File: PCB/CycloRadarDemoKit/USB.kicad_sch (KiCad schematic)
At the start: 9 parts, among them J301 USB_C_Receptacle_USB2.0, U301 CP2102N-Axx-xQFN28

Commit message: USB designed with TODOs, ESP part changed
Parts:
- added D302: TX_LED, symbol Device:LED
- added D303: RX_LED, symbol Device:LED
- added Q301, Q302: L8050QLT1G, Package_TO_SOT_SMD:SOT-23, symbol Transistor_BJT:BC817
- added R302: 22.1K(1%), symbol Device:R
- added R303: 47.5K(1%), symbol Device:R
- added R304, R305: ???, symbol Device:R
- added R306, R307: 100K(1%), symbol Device:R
- R301: value 4.7K(1%) -> 1K(1%)
- U301: footprint Package_DFN_QFN:QFN-28-1EP_5x5mm_P0.5mm_EP3.35x3.35mm -> Package_DFN_QFN:QFN-24-1EP_4x4mm_P0.5mm_EP2.6x2.6mm; symbol Interface_USB:CP2102N-Axx-xQFN28 -> Interface_USB:CP2102N-Axx-xQFN24
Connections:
- net +3V3_USB: now also U301.5 (VIO), D302.2 (A), D303.2 (A)
- net EN_AUTO: now also Q301.3 (C)
- net GND: now also U301.2 (GND), U301.25 (GND), R303.2; no longer U301.29 (GND), U301.3 (GND)
- net IO0_AUTO: now also Q302.3 (C)
- net RXD: now also U301.20 (RXD); no longer U301.25 (RXD)
- net TXD: now also U301.21 (TXD); no longer U301.26 (TXD)
- net VBUS: now also R302.1; no longer U301.8 (VBUS)
- net at U301.13 (~{RXT}/GPIO.1): now also R305.1
- net at U301.14 (~{TXT}/GPIO.0): now also R304.1
- net RTS: now reaches U301.19 (~{RTS})
- net RTS: now also Q301.2 (E), R307.1
- net DTR: now reaches U301.23 (~{DTR})
- net DTR: now also Q302.2 (E), R306.1
- net at D301.4 (K), J301.A6 (D+), J301.B6 (D+): now also U301.3 (D+); no longer U301.4 (D+)
- net at D301.3 (K), J301.A7 (D-), J301.B7 (D-): now also U301.4 (D-); no longer U301.5 (D-)
- new net: D303.1 (K), R305.2
- new net: R302.2, R303.1, U301.8 (VBUS)
- new net: Q302.1 (B), R307.2
- new net: Q301.1 (B), R306.2
- new net: D302.1 (K), R304.2
- no-connect marks 5 -> 13
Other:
- note added: "TODO: Choose LEDs and their resistors"
- note removed: "TODO: AUTO BOOT"
- note removed: "TODO: Compare the circuity with the ESP32 module schematics"
- moved on the sheet: C301, C302, C303, C304, D301, FB301, J301, R301

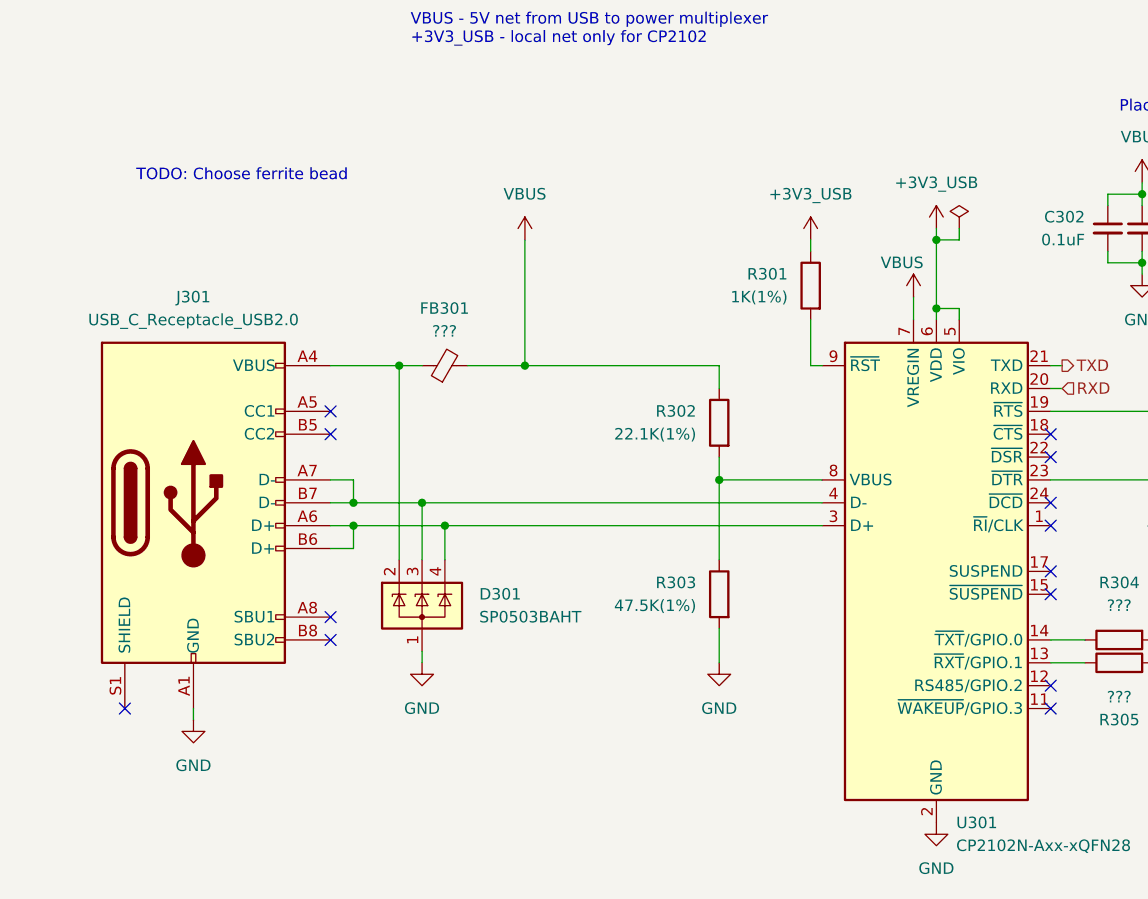
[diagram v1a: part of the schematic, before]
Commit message: Readme, PCB new symbol routed
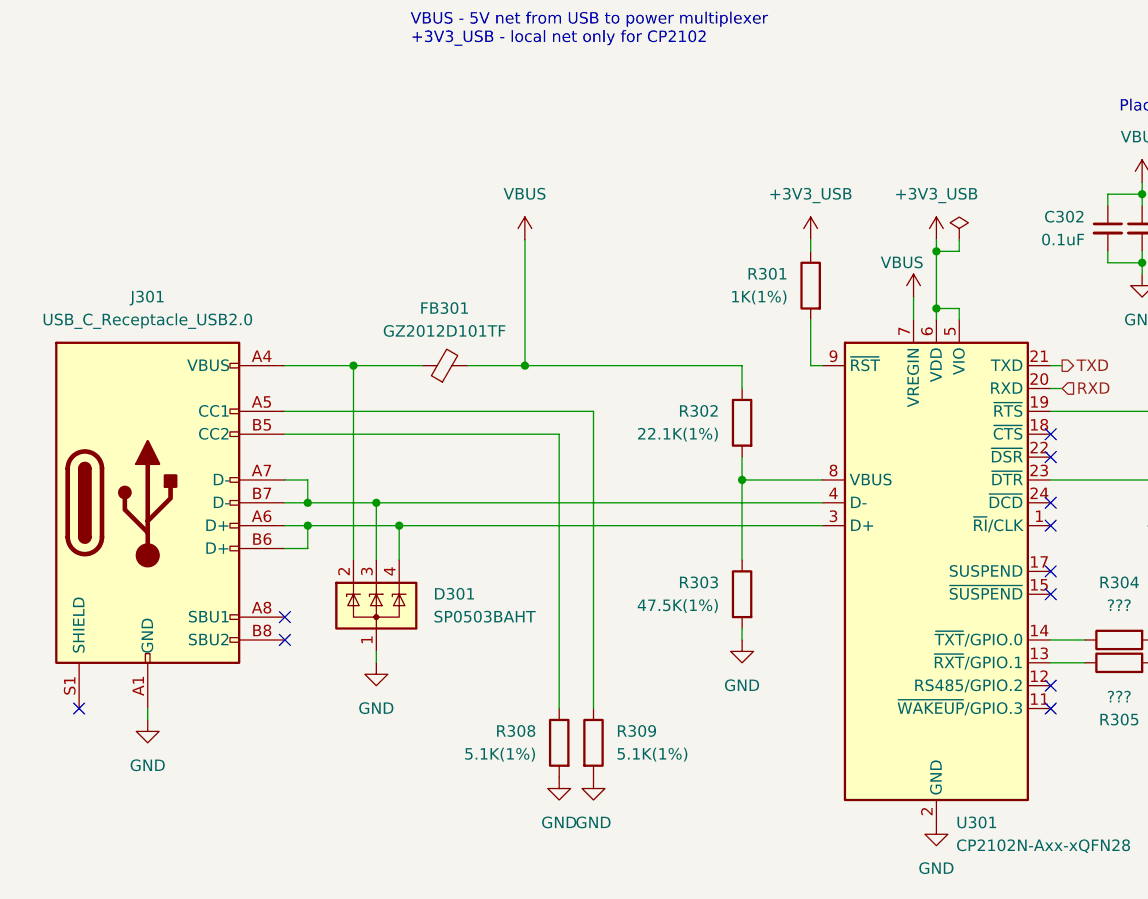
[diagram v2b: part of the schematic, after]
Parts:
- added R308, R309: 5.1K(1%), symbol Device:R
- FB301: value ??? -> GZ2012D101TF
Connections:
- net GND: now also R308.2, R309.2
- net at J301.A5 (CC1): now also R309.1
- net at J301.B5 (CC2): now also R308.1
- no-connect marks 13 -> 11
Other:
- note removed: "TODO: Choose ferrite bead"
- moved on the sheet: D301, J301, R302, R303

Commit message: PCB power manag. WIP
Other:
- note added: "Notes: +3V3_USB - local net only for CP2102 VBUS - 5V net from USB to power multiplexer"
- note removed: "Notes: Max current through VDD: 500mA VBUS - 5V net from USB to power multiplexer +3V3_USB - local net only for CP2102"
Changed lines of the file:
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@@
     (stroke (width 0) (type default))
   )
-  (text "Notes:\nMax current through VDD: 500mA\n\nVBUS - 5V net from USB to power multiplexer\n+3V3_USB - local net only for CP2102"
-    (at 88.9 33.02 0)
+  (text "Notes:\n+3V3_USB - local net only for CP2102\nVBUS - 5V net from USB to power multiplexer"
+    (at 105.41 38.1 0)
     (effects (font (size 1.27 1.27)) (justify left bottom))
   )

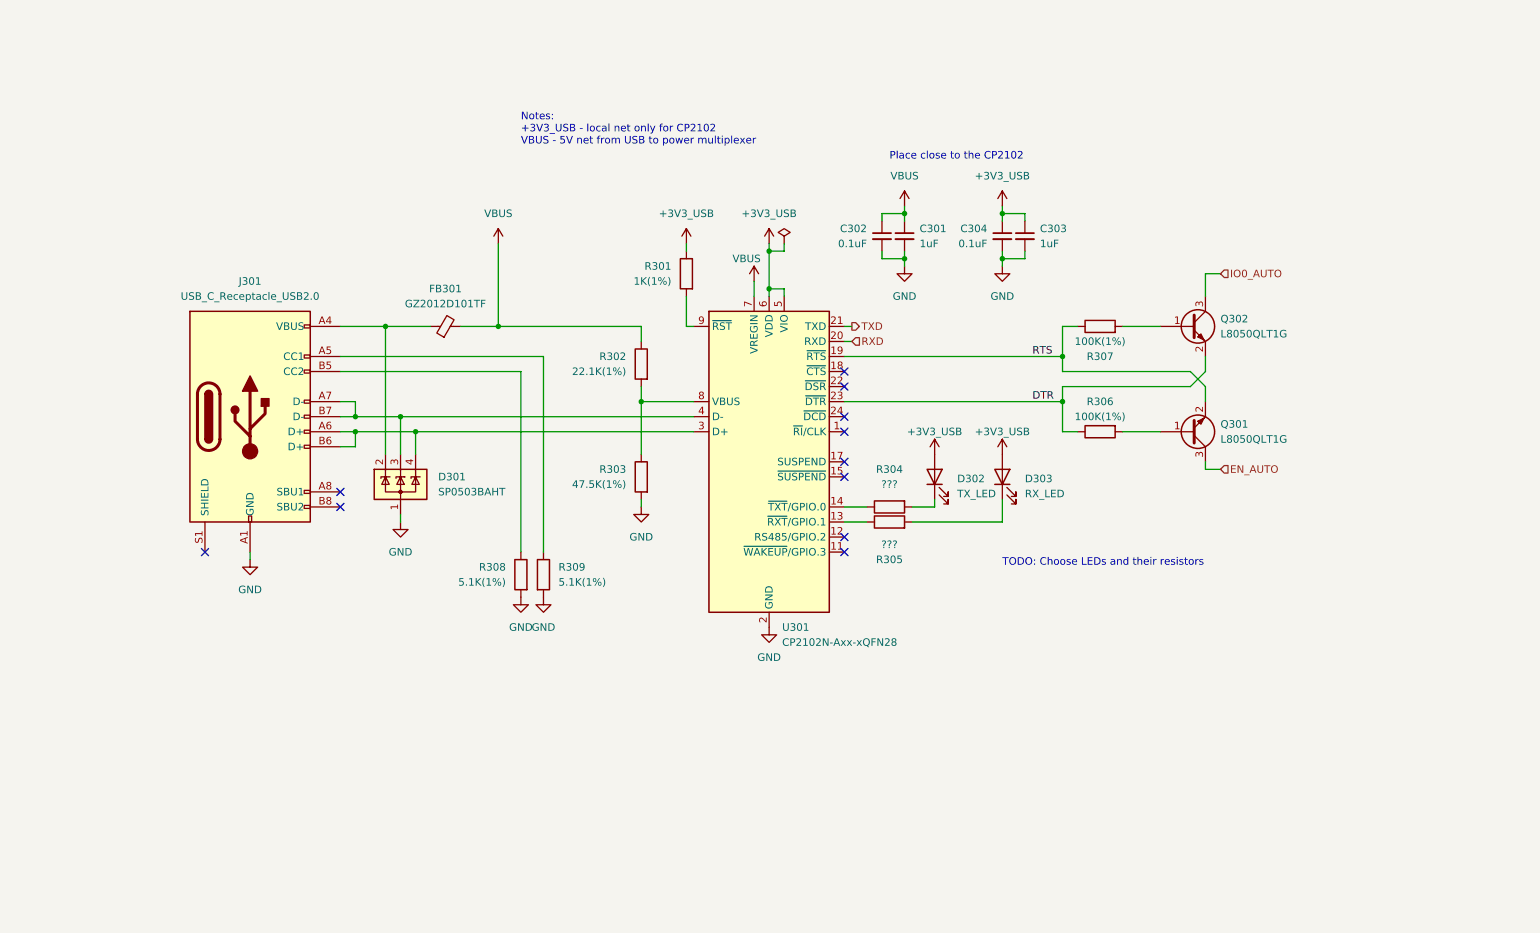
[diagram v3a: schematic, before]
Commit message: Power management almost done
5V/3.3V changed to AP63203
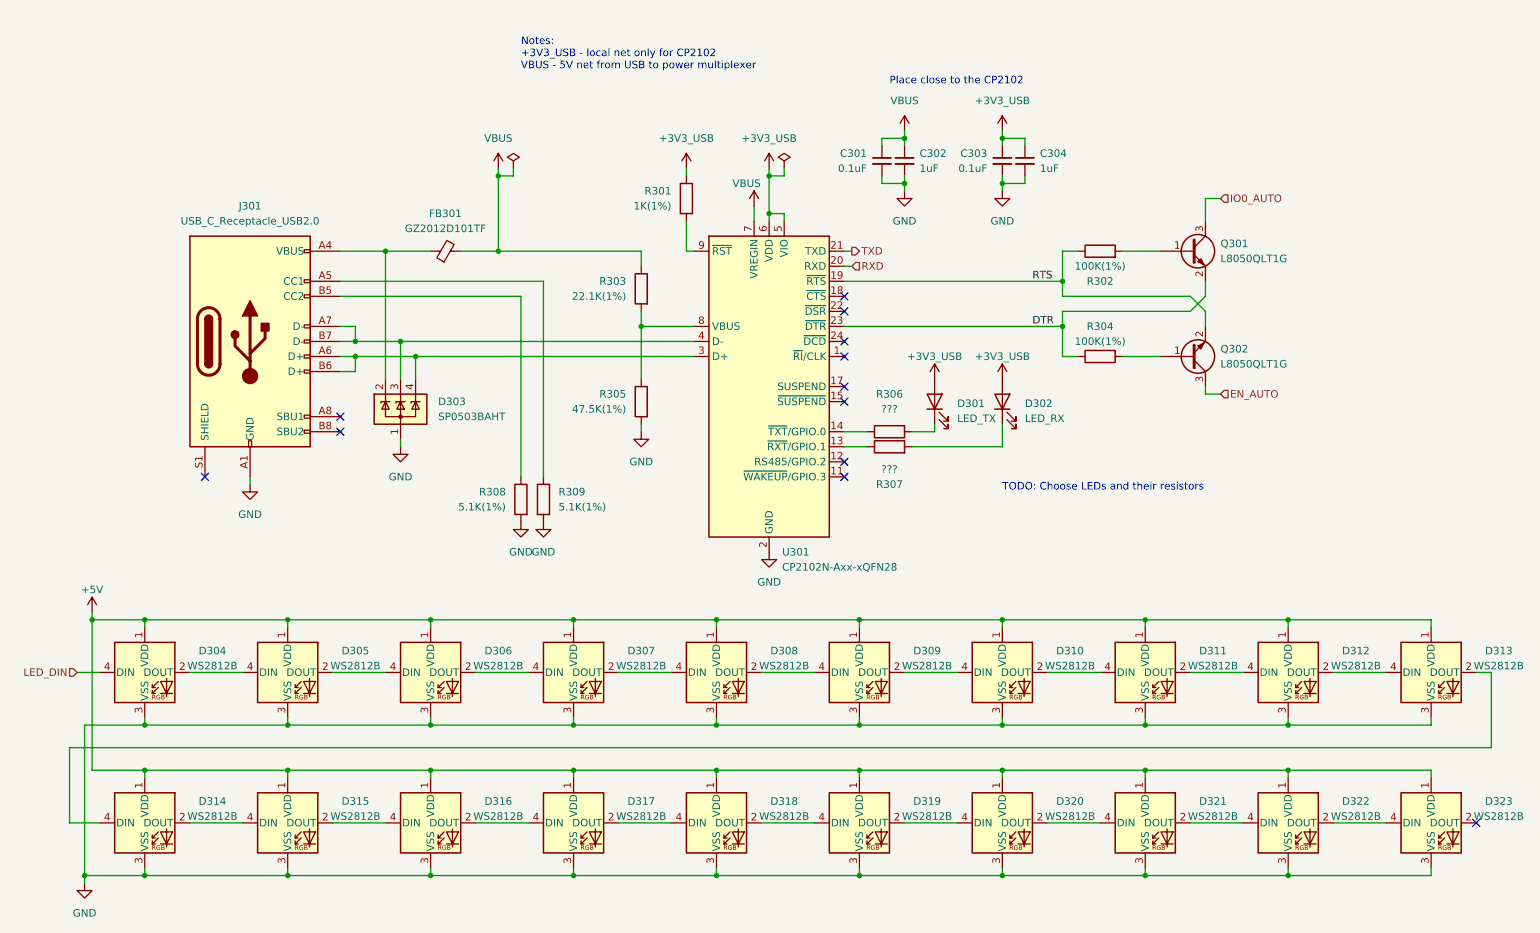
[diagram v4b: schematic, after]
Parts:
- added D304, D305, D306, D307, D308, D309, D310, D311, D312, D313, D314, D315, D316, D317, D318, D319, D320, D321, D322, D323: WS2812B, LED_SMD:LED_SK6812MINI_PLCC4_3.5x3.5mm_P1.75mm, symbol LED:WS2812B
- D301: renamed from D302; value TX_LED -> LED_TX
- D302: renamed from D303; value RX_LED -> LED_RX
- renumbered C302 to C301, C301 to C302, C304 to C303, C303 to C304, D301 to D303, Q302 to Q301, Q301 to Q302, R307 to R302, R302 to R303, R306 to R304, R303 to R305, R304 to R306, R305 to R307
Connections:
- net GND: now also D304.3 (VSS), D305.3 (VSS), D306.3 (VSS), D307.3 (VSS), D308.3 (VSS), D309.3 (VSS), D310.3 (VSS), D311.3 (VSS), D312.3 (VSS), D313.3 (VSS), D314.3 (VSS), D315.3 (VSS), D316.3 (VSS), D317.3 (VSS), D318.3 (VSS), D319.3 (VSS), D320.3 (VSS), D321.3 (VSS), D322.3 (VSS), D323.3 (VSS)
- new net: D321.2 (DOUT), D322.4 (DIN)
- new net: D320.2 (DOUT), D321.4 (DIN)
- new net: D307.2 (DOUT), D308.4 (DIN)
- new net: D306.2 (DOUT), D307.4 (DIN)
- new net: D315.2 (DOUT), D316.4 (DIN)
- new net: D314.2 (DOUT), D315.4 (DIN)
- new net: D309.2 (DOUT), D310.4 (DIN)
- new net: D308.2 (DOUT), D309.4 (DIN)
- new net: D310.2 (DOUT), D311.4 (DIN)
- new net: D305.2 (DOUT), D306.4 (DIN)
- new net: D304.2 (DOUT), D305.4 (DIN)
- new net: D322.2 (DOUT), D323.4 (DIN)
- new net: D319.2 (DOUT), D320.4 (DIN)
- new net: D318.2 (DOUT), D319.4 (DIN)
- new net: D317.2 (DOUT), D318.4 (DIN)
- new net: D316.2 (DOUT), D317.4 (DIN)
- new net: D311.2 (DOUT), D312.4 (DIN)
- new net: D313.2 (DOUT), D314.4 (DIN)
- new net: D312.2 (DOUT), D313.4 (DIN)
- new net +5V: D304.1 (VDD), D305.1 (VDD), D306.1 (VDD), D307.1 (VDD), D308.1 (VDD), D309.1 (VDD), D310.1 (VDD), D311.1 (VDD), D312.1 (VDD), D313.1 (VDD), D314.1 (VDD), D315.1 (VDD), D316.1 (VDD), D317.1 (VDD), D318.1 (VDD), D319.1 (VDD), D320.1 (VDD), D321.1 (VDD), D322.1 (VDD), D323.1 (VDD)
- new net LED_DIN: D304.4 (DIN)
- no-connect marks 11 -> 12
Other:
- moved on the sheet: C301, C302, C303, C304, D301, D302, D303, FB301, J301, Q301, Q302, R301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

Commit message: RJ45 chose, leds connected
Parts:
- C301, C303: value 0.1uF -> 0.1uF/50V(10%); footprint (none) -> Capacitor_SMD:C_0603_1608Metric; LCSC (none) -> C14663
- C302, C304: value 1uF -> 1uF/50V(10%); footprint (none) -> Capacitor_SMD:C_0603_1608Metric; LCSC (none) -> C15849
- D303: LCSC (none) -> C2682275
- Q301, Q302: LCSC (none) -> C49581
- R308, R309: value 5.1K(1%) -> 5.1K(5%)
- U301: LCSC (none) -> C964632
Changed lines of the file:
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@@
         )
         (path "/c2cd7ca4-4652-4b3d-a3a8-1cfa66cb11e9/db1e19a0-821c-4756-9ad0-6b0269412516"
-          (reference "#FLG0302") (unit 1)
+          (reference "#FLG0301") (unit 1)
         )
       )
@@
     )
     (property "Datasheet" "https://www.silabs.com/documents/public/data-sheets/cp2102n-datasheet.pdf" (at 148.59 97.79 0)
+      (effects (font (size 1.27 1.27)) hide)
+    )
+    (property "LCSC" "C964632" (at 147.32 78.74 0)
       (effects (font (size 1.27 1.27)) hide)
     )
@@
       (effects (font (size 1.27 1.27)) (justify left) hide)
     )
+    (property "LCSC" "C49581" (at 218.44 55.88 0)
+      (effects (font (size 1.27 1.27)) hide)
+    )
     (pin "1")
     (pin "3")
@@
       (effects (font (size 1.27 1.27)) (justify left))
     )
-    (property "Value" "5.1K(1%)" (at 111.76 99.06 0)
+    (property "Value" "5.1K(5%)" (at 111.76 99.06 0)
       (effects (font (size 1.27 1.27)) (justify left))
     )
@@
       (effects (font (size 1.27 1.27)) (justify left) hide)
     )
+    (property "LCSC" "C49581" (at 218.44 73.66 0)
+      (effects (font (size 1.27 1.27)) hide)
+    )
     (pin "1")
     (pin "3")
@@
       (effects (font (size 1.27 1.27)) (justify left))
     )
-    (property "Value" "1uF" (at 193.04 41.9163 0)
-      (effects (font (size 1.27 1.27)) (justify left))
-    )
-    (property "Footprint" "" (at 190.5 40.64 0)
+    (property "Value" "1uF/50V(10%)" (at 193.04 41.9163 0)
+      (effects (font (size 1.27 1.27)) (justify left))
+    )
+    (property "Footprint" "Capacitor_SMD:C_0603_1608Metric" (at 190.5 40.64 0)
       (effects (font (size 1.27 1.27)) hide)
     )
@@
       (effects (font (size 1.27 1.27)) hide)
     )
+    (property "LCSC" "C15849" (at 190.5 40.64 0)
+      (effects (font (size 1.27 1.27)) hide)
+    )
     (pin "2")
     (pin "1")
@@
       (effects (font (size 1.27 1.27)) (justify left))
     )
-    (property "Value" "0.1uF" (at 163.83 41.9163 0)
-      (effects (font (size 1.27 1.27)) (justify left))
-    )
-    (property "Footprint" "" (at 166.37 40.64 0)
+    (property "Value" "0.1uF/50V(10%)" (at 163.83 41.9163 0)
+      (effects (font (size 1.27 1.27)) (justify left))
+    )
+    (property "Footprint" "Capacitor_SMD:C_0603_1608Metric" (at 166.37 40.64 0)
       (effects (font (size 1.27 1.27)) hide)
     )
@@
       (effects (font (size 1.27 1.27)) hide)
     )
+    (property "LCSC" "C14663" (at 166.37 40.64 0)
+      (effects (font (size 1.27 1.27)) hide)
+    )
     (pin "2")
     (pin "1")
@@
   (symbol (lib_id "power:PWR_FLAG") (at 149.86 41.91 0) (unit 1)
     (in_bom yes) (on_board yes) (dnp no) (fields_autoplaced)
-    (property "Reference" "#FLG0301" (at 149.86 40.005 0)
+    (property "Reference" "#FLG0302" (at 149.86 40.005 0)
       (effects (font (size 1.27 1.27)) hide)
     )
@@
       (project "CycloRadarDemoKit"
         (path "/c2cd7ca4-4652-4b3d-a3a8-1cfa66cb11e9/db1e19a0-821c-4756-9ad0-6b0269412516"
-          (reference "#FLG0301") (unit 1)
+          (reference "#FLG0302") (unit 1)
         )
       )
@@
       (effects (font (size 1.27 1.27)) (justify left))
     )
-    (property "Value" "0.1uF" (at 184.15 41.9163 0)
-      (effects (font (size 1.27 1.27)) (justify left))
-    )
-    (property "Footprint" "" (at 186.69 40.64 0)
+    (property "Value" "0.1uF/50V(10%)" (at 184.15 41.9163 0)
+      (effects (font (size 1.27 1.27)) (justify left))
+    )
+    (property "Footprint" "Capacitor_SMD:C_0603_1608Metric" (at 186.69 40.64 0)
       (effects (font (size 1.27 1.27)) hide)
     )
     (property "Datasheet" "~" (at 186.69 40.64 0)
+      (effects (font (size 1.27 1.27)) hide)
+    )
+    (property "LCSC" "C14663" (at 186.69 40.64 0)
       (effects (font (size 1.27 1.27)) hide)
     )
@@
       (effects (font (size 1.27 1.27)) (justify left) hide)
     )
-    (property "Datasheet" "http://www.littelfuse.com/~/media/files/littelfuse/technical%20resources/documents/data%20sheets/sp05xxba.pdf" (at 88.265 79.375 0)
+    (property "Datasheet" "https://datasheet.lcsc.com/lcsc/2108132030_TECH-PUBLIC-TPSP0503BAHTG_C2682275.pdf" (at 88.265 79.375 0)
+      (effects (font (size 1.27 1.27)) hide)
+    )
+    (property "LCSC" "C2682275" (at 85.09 82.55 0)
       (effects (font (size 1.27 1.27)) hide)
     )
@@
       (effects (font (size 1.27 1.27)) (justify left))
     )
-    (property "Value" "1uF" (at 172.72 41.9163 0)
-      (effects (font (size 1.27 1.27)) (justify left))
-    )
-    (property "Footprint" "" (at 170.18 40.64 0)
+    (property "Value" "1uF/50V(10%)" (at 172.72 41.9163 0)
+      (effects (font (size 1.27 1.27)) (justify left))
+    )
+    (property "Footprint" "Capacitor_SMD:C_0603_1608Metric" (at 170.18 40.64 0)
       (effects (font (size 1.27 1.27)) hide)
     )
     (property "Datasheet" "~" (at 170.18 40.64 0)
+      (effects (font (size 1.27 1.27)) hide)
+    )
+    (property "LCSC" "C15849" (at 170.18 40.64 0)
       (effects (font (size 1.27 1.27)) hide)
     )
@@
       (effects (font (size 1.27 1.27)) (justify left))
     )
-    (property "Value" "5.1K(1%)" (at 102.87 99.06 0)
-      (effects (font (size 1.27 1.27)) (justify left))
-    )
+    (property "Value" "5.1K(5%)" (at 102.87 99.06 0)
+      (effects (font (size 1.27 1.27)) (justify left))
+    )

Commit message: MCU routed, two GPIO tested
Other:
- moved on the sheet: C301, C302, C303, C304
